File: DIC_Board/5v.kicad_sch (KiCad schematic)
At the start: 8 parts, among them J30 0430450200, U30 TPS27S100APWPR

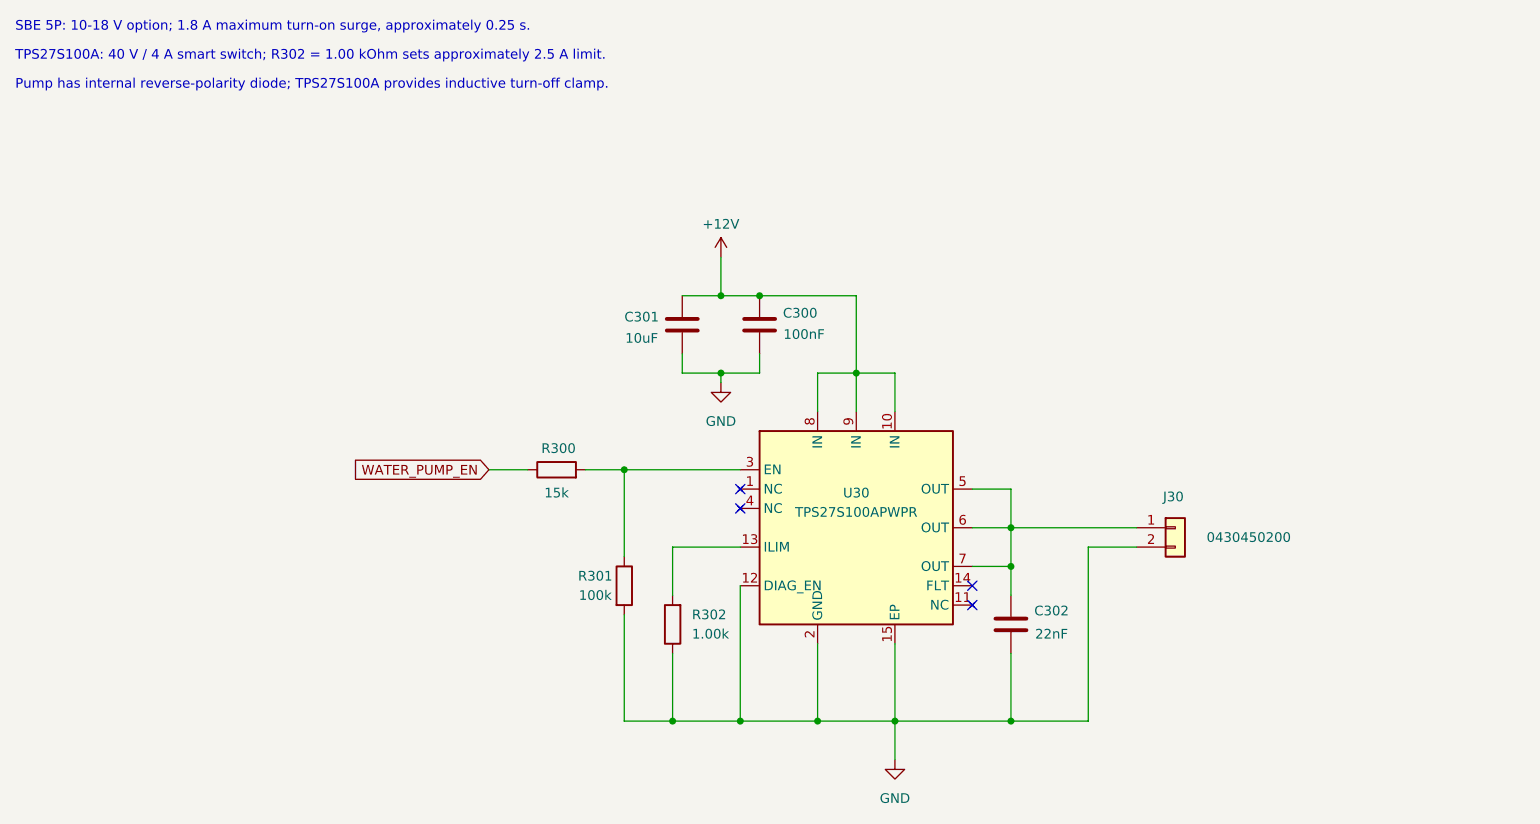
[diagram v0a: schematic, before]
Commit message: Separated the power sheets, did the sensor sheets.
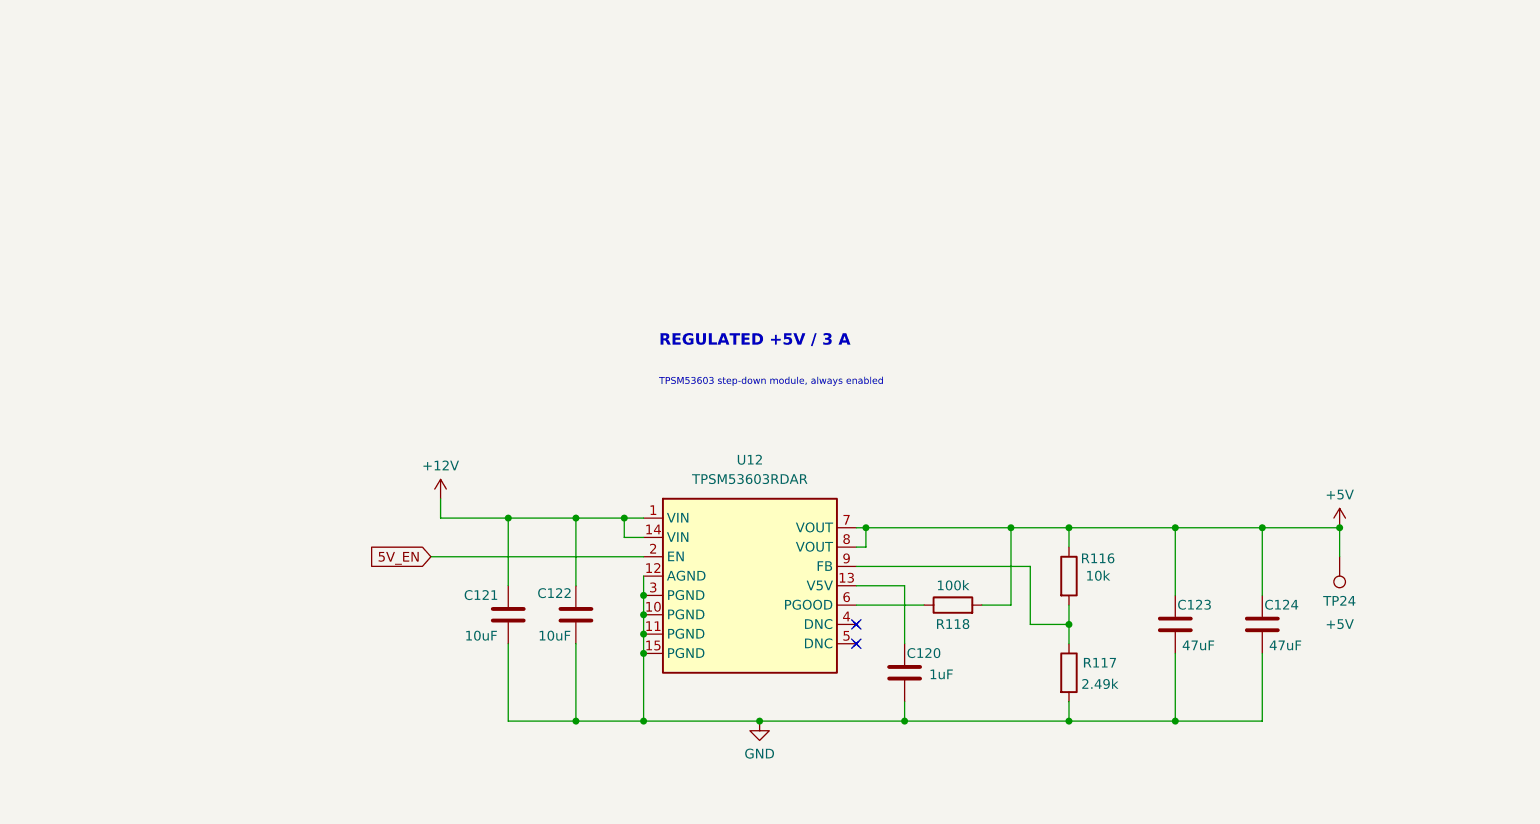
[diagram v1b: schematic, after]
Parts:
- removed C300: 100nF, Capacitor_SMD:C_0402_1005Metric, symbol Device:C
- removed C301: 10uF, Capacitor_SMD:C_1206_3216Metric, symbol Device:C
- removed C302: 22nF, Capacitor_SMD:C_0402_1005Metric, symbol Device:C
- removed J30: 0430450200, Connector_Molex:Molex_Micro-Fit_3.0_43045-0200_2x01_P3.00mm_Horizontal, symbol Connector_Generic:Conn_01x02
- removed R300: 15k, Resistor_SMD:R_0402_1005Metric, symbol Device:R
- removed R301: 100k, Resistor_SMD:R_0402_1005Metric, symbol Device:R
- removed R302: 1.00k, Resistor_SMD:R_0402_1005Metric, symbol Device:R
- removed U30: TPS27S100APWPR, Package_SO:Texas_HTSSOP-14-1EP_4.4x5mm_P0.65mm_EP3.4x5mm_Mask3.155x3.255mm_ThermalVias, symbol DIC_Board:TPS27S100A
- added C120: 1uF, Capacitor_SMD:C_0603_1608Metric, symbol Device:C
- added C121, C122: 10uF, Capacitor_SMD:C_1206_3216Metric, symbol Device:C
- added C123, C124: 47uF, Capacitor_SMD:C_1210_3225Metric, symbol Device:C
- added R116: 10k, Resistor_SMD:R_0402_1005Metric, symbol Device:R
- added R117: 2.49k, Resistor_SMD:R_0402_1005Metric, symbol Device:R
- added R118: 100k, Resistor_SMD:R_0402_1005Metric, symbol Device:R
- added TP24: +5V, TestPoint:TestPoint_Plated_Hole_D2.0mm, symbol Connector:TestPoint
- added U12: TPSM53603RDAR, Package_DFN_QFN:Texas_B3QFN-14-1EP_5x5.5mm_P0.65mm_ThermalVia, symbol DIC_Board:TPSM53603RDA
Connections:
- net +12V: now also C121.1, C122.1, U12.1 (VIN), U12.14 (VIN)
- net GND: now also C120.2, C121.2, C122.2, C123.2, C124.2, R117.2, U12.10 (PGND), U12.11 (PGND), U12.12 (AGND), U12.15 (PGND), U12.3 (PGND)
- new net: C120.1, U12.13 (V5V)
- new net: R118.1, U12.6 (PGOOD)
- new net: R116.2, R117.1, U12.9 (FB)
- new net +5V: C123.1, C124.1, R116.1, R118.2, TP24.1, U12.7 (VOUT), U12.8 (VOUT)
- new net 5V_EN: U12.2 (EN)
- no-connect marks 4 -> 2
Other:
- note added: "REGULATED +5V / 3 A"
- note added: "TPSM53603 step-down module, always enabled"
- note removed: "Pump has internal reverse-polarity diode; TPS27S100A provides inductive turn-off clamp."
- note removed: "SBE 5P: 10-18 V option; 1.8 A maximum turn-on surge, approximately 0.25 s."
- note removed: "TPS27S100A: 40 V / 4 A smart switch; R302 = 1.00 kOhm sets approximately 2.5 A limit."
- title: Water Pump -> (none)

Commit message: Synchronize schematic hierarchy and MCU pin map
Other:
- note added: "TPSM53603 step-down module; default-on, MCU-controllable"
- note removed: "TPSM53603 step-down module, always enabled"
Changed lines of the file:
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@@
 	(generator_version "10.0")
 	(paper "A4")
-	(text "TPSM53603 step-down module, always enabled"
+	(text "TPSM53603 step-down module; default-on, MCU-controllable"
 		(exclude_from_sim no)
 		(at 113.792 70.358 0)
@@
 		)
 	)
-	(global_label "5V_EN"
+	(hierarchical_label "5V_EN"
 		(shape input)
 		(at 83.82 92.71 180)
-		(fields_autoplaced yes)
 		(effects
 			(font
@@
 			(justify right)
 		)
-		(property "Intersheetrefs" "${INTERSHEET_REFS}"
-			(at 75.0896 92.71 0)
-			(hide yes)
-			(show_name no)
-			(do_not_autoplace no)
-			(effects
-				(font
-					(size 1.27 1.27)
-				)
-				(justify right)
-			)
-		)
-	)
+	)

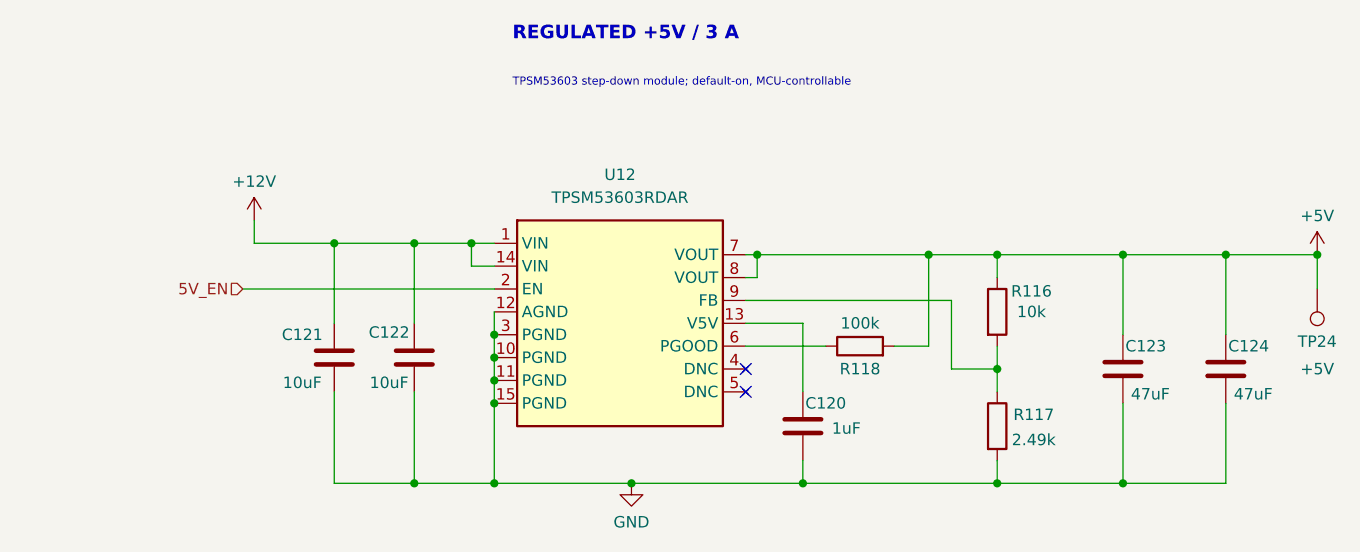
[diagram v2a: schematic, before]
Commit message: Synchronize power, communications, and MCU configuration
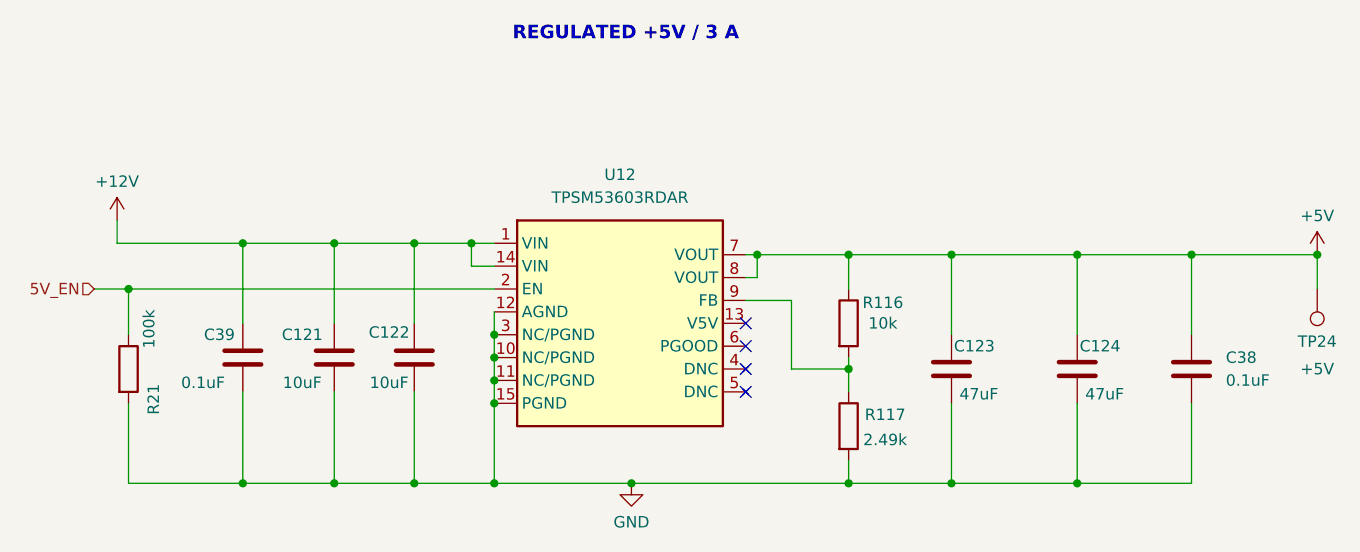
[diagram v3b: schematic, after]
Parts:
- removed C120: 1uF, Capacitor_SMD:C_0603_1608Metric, symbol Device:C
- removed R118: 100k, Resistor_SMD:R_0402_1005Metric, symbol Device:R
- added C38, C39: 0.1uF, symbol Device:C
- added R21: 100k, Resistor_SMD:R_0402_1005Metric, symbol Device:R
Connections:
- net +12V: now also C39.1
- net +5V: now also C38.1
- net 5V_EN: now also R21.1
- net GND: now also C38.2, C39.2, R21.2
- no-connect marks 2 -> 4
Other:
- note removed: "TPSM53603 step-down module; default-on, MCU-controllable"
- moved on the sheet: C123, C124, R116, R117

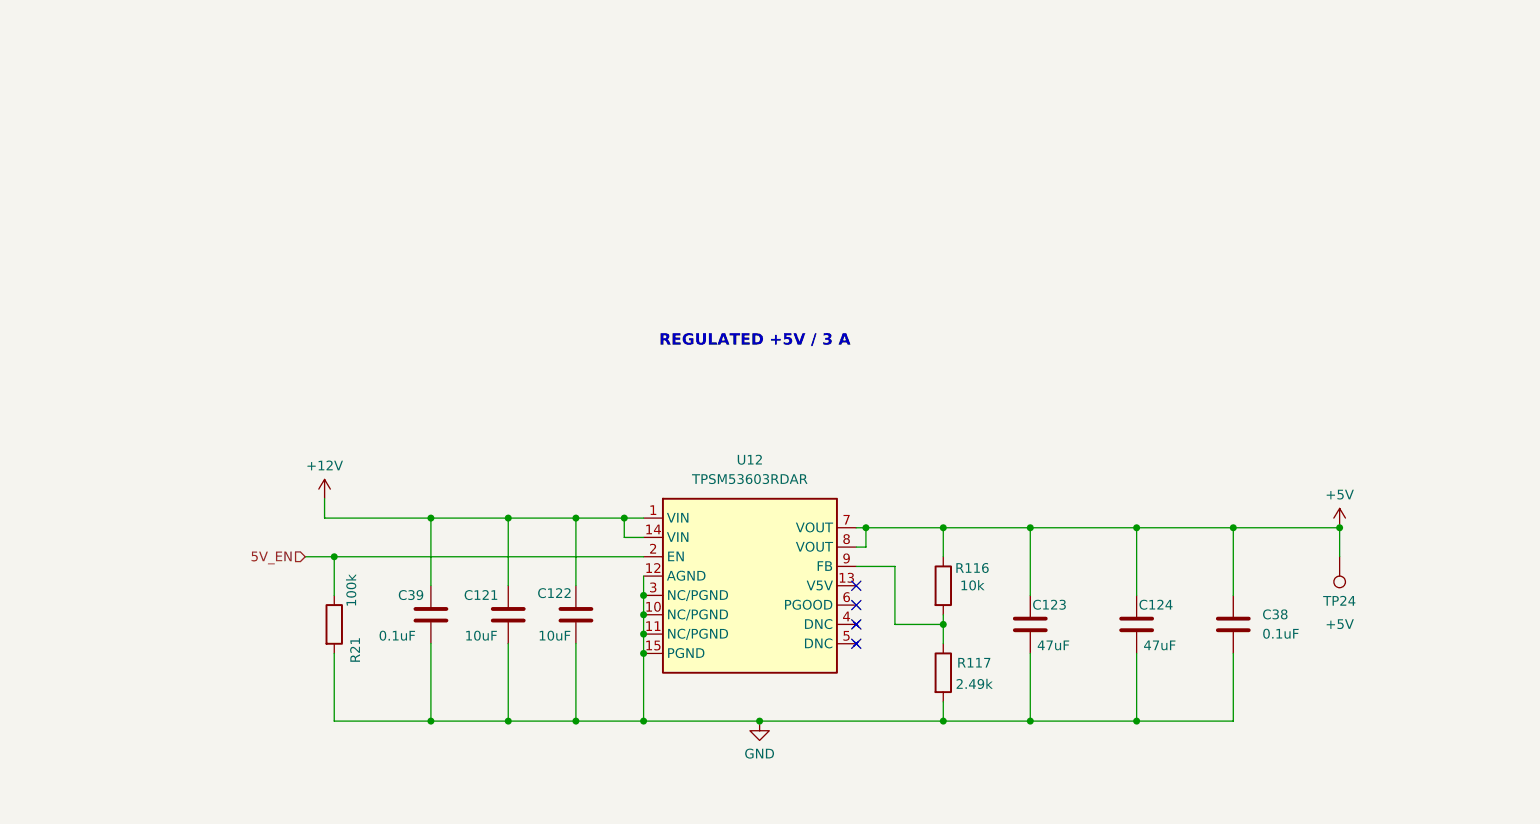
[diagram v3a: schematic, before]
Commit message: Updated board for layout! All footprints added
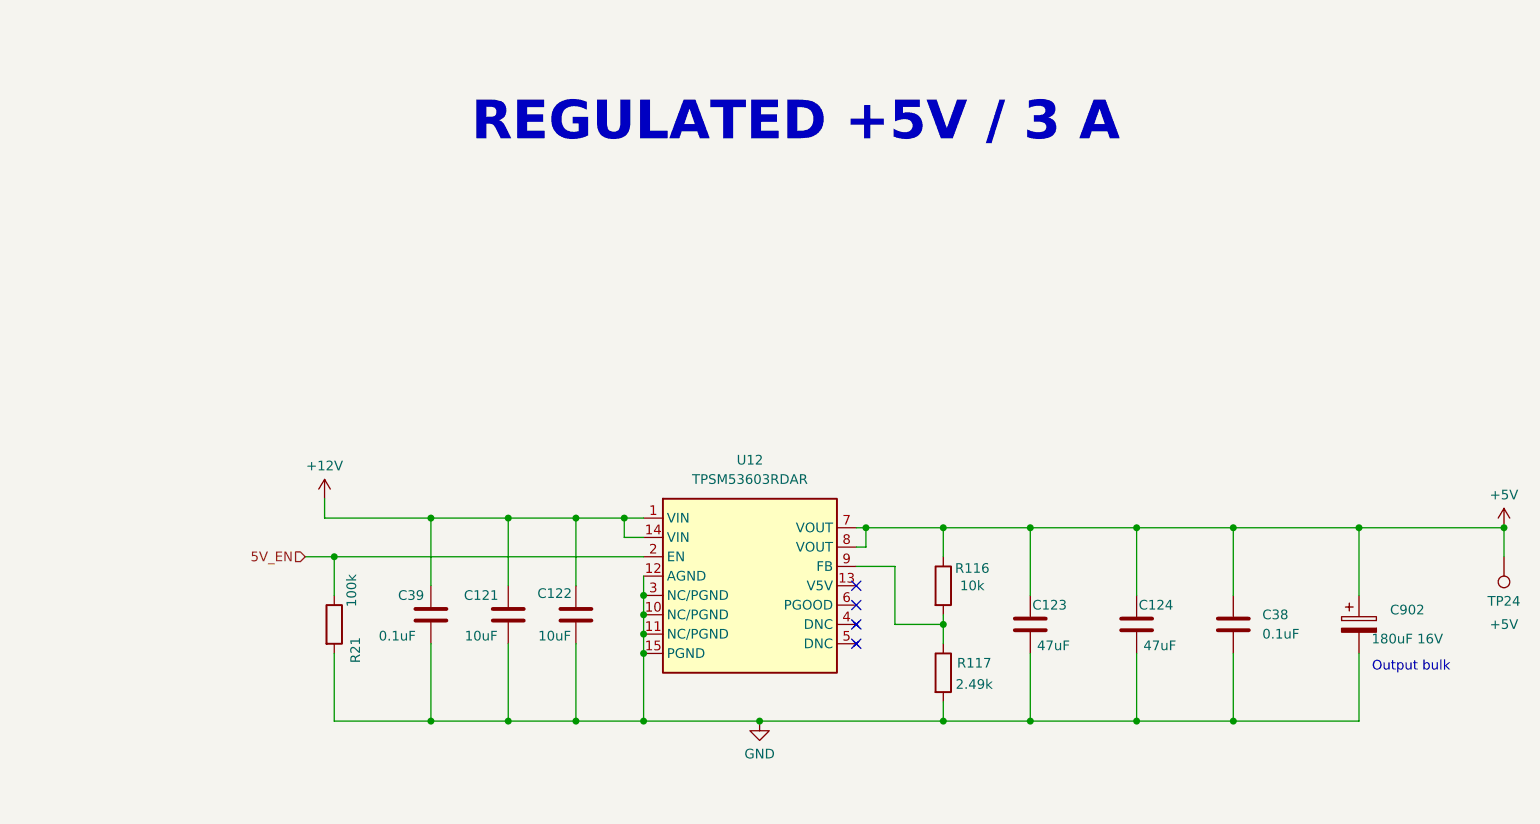
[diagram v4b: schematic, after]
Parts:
- added C902: 180uF 16V, Capacitor_SMD:CP_Elec_6.3x5.9, symbol Device:C_Polarized
- C38, C39: footprint (none) -> Capacitor_SMD:C_0603_1608Metric; BOM Source (none) -> https://product.tdk.com/en/search/capacitor/ceramic/mlcc/in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; Dielectric (none) -> X7R; MPN (none) -> C1608X7R1H104K080AA; Manufacturer (none) -> TDK; Tolerance (none) -> 10%; Voltage Rating (none) -> 50V
- TP24: now left out of the parts list
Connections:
- net +5V: now also C902.1
- net GND: now also C902.2
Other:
- note added: "Output bulk"
- moved on the sheet: TP24

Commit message: Let gpt6 astra have a go at routing. bad results.
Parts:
- TP24: footprint TestPoint:TestPoint_Plated_Hole_D2.0mm -> TestPoint:TestPoint_Pad_D1.0mm
- U12: footprint Package_DFN_QFN:Texas_B3QFN-14-1EP_5x5.5mm_P0.65mm_ThermalVia -> DIC_Board:TPSM53603_Thermal_Drill0p3
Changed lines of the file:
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@@
 			)
 		)
-		(property "Footprint" "Package_DFN_QFN:Texas_B3QFN-14-1EP_5x5.5mm_P0.65mm_ThermalVia"
+		(property "Footprint" "DIC_Board:TPSM53603_Thermal_Drill0p3"
 			(at 125.73 96.52 0)
 			(hide yes)
@@
 			)
 		)
-		(property "Footprint" "TestPoint:TestPoint_Plated_Hole_D2.0mm"
+		(property "Footprint" "TestPoint:TestPoint_Pad_D1.0mm"
 			(at 224.79 92.71 0)
 			(hide yes)
